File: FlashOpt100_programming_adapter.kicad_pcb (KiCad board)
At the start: 2 copper layers, 17.8 x 35.6 mm, 3 parts, among them J1 29F256 / 29C256, J2 FlashOpt100_PRG_4x7

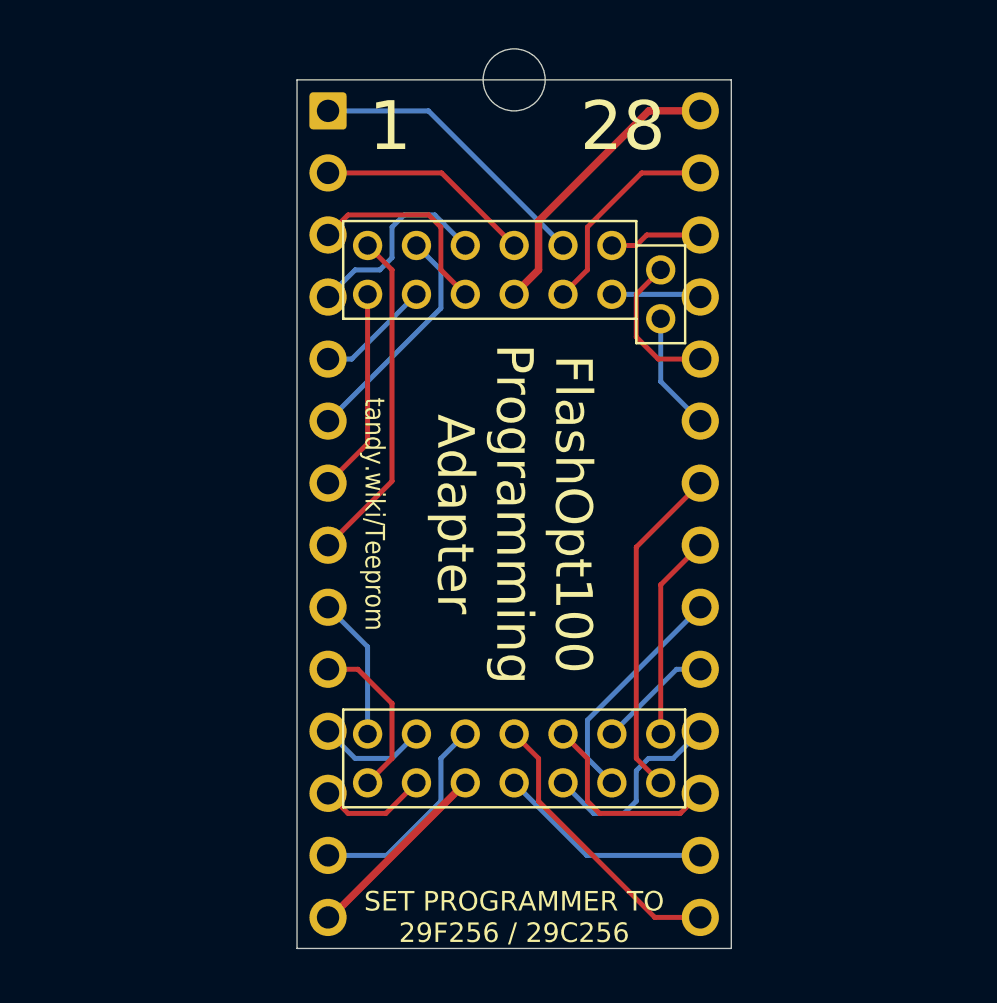
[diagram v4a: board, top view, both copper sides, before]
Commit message: kicad 6, flashopt100 programming socket
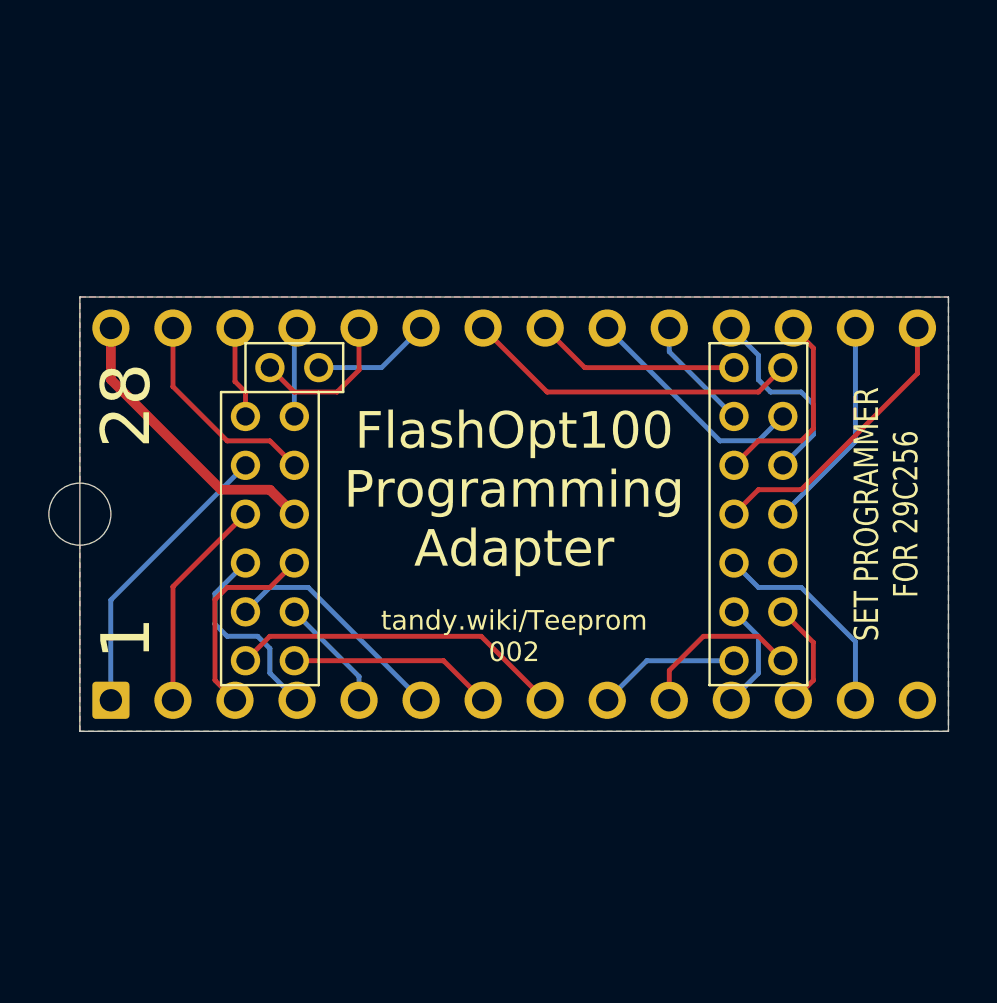
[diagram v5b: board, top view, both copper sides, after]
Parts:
- moved notch 25.1 mm to (129.4, 99.2), turned to 90 degrees
- turned J1 to 90 degrees
- turned J2 to 0 degrees
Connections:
- net /~CE renamed /~{CE}
- net /~OE renamed /~{OE}
- net /~WE renamed /~{WE}
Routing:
- net GND: track 7.90 -> 0.11 mm
- added copper zone on B.Cu, net GND
- added copper zone on F.Cu, net GND
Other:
- board size 17.8 x 35.6 mm -> 35.6 x 17.8 mm
- net class Default removed
- board text added: "${COMMENT2} ${REVISION}"
- board text added: "SET PROGRAMMER FOR 29C256"
- board text removed: "SET PROGRAMMER TO 29F256 / 29C256"
- board text removed: "tandy.wiki/Teeprom"
